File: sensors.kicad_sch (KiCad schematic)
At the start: 22 parts, among them J10 DISTANCE_R90, J11 DISTANCE_R, J12 DISTANCE_RF, J13 DISTANCE_L90, J14 DISTANCE_L, J15 LINE_LEFT, J16 DISTANCE_LF, J8 DISTANCE_CENTER, J9 LINE_RIGHT, U5 TXS0108EPWR

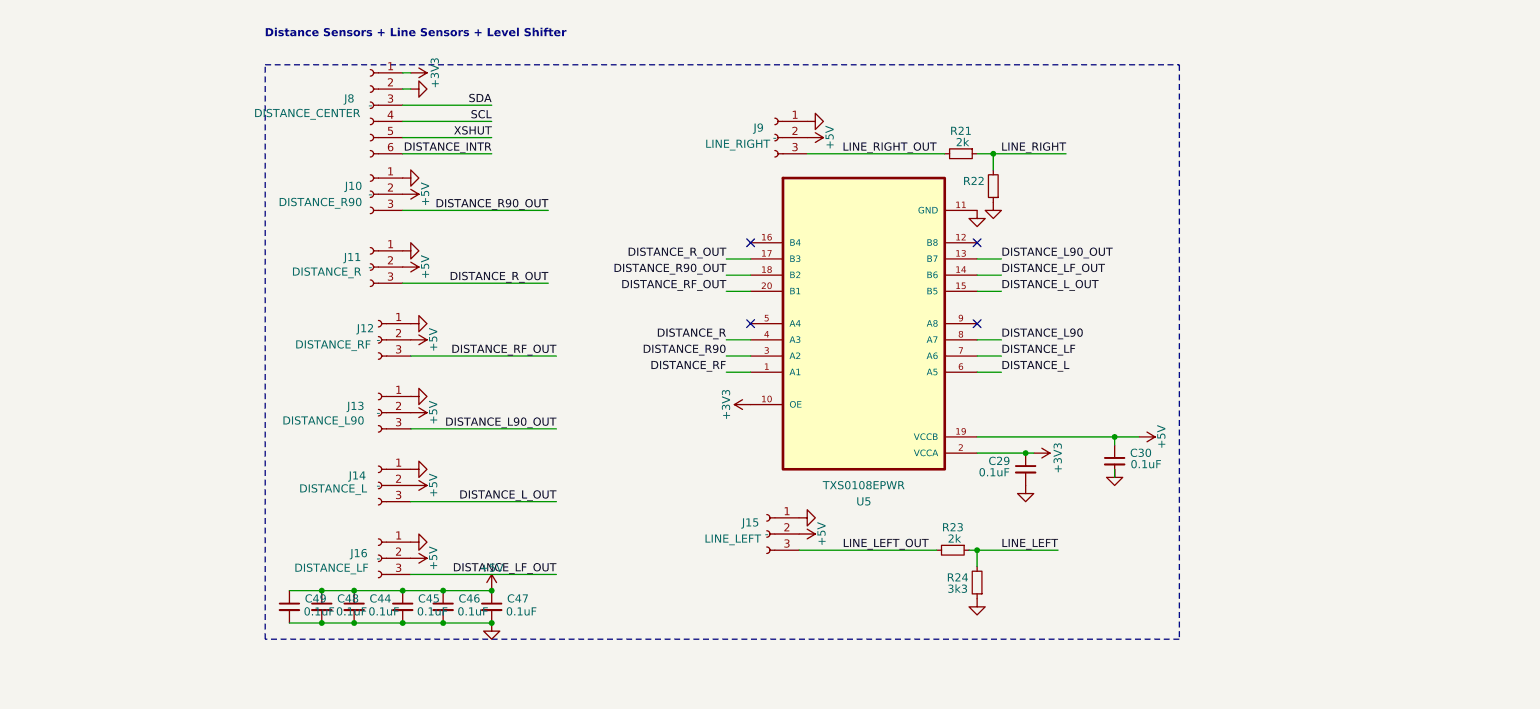
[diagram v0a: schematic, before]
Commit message: added global labels
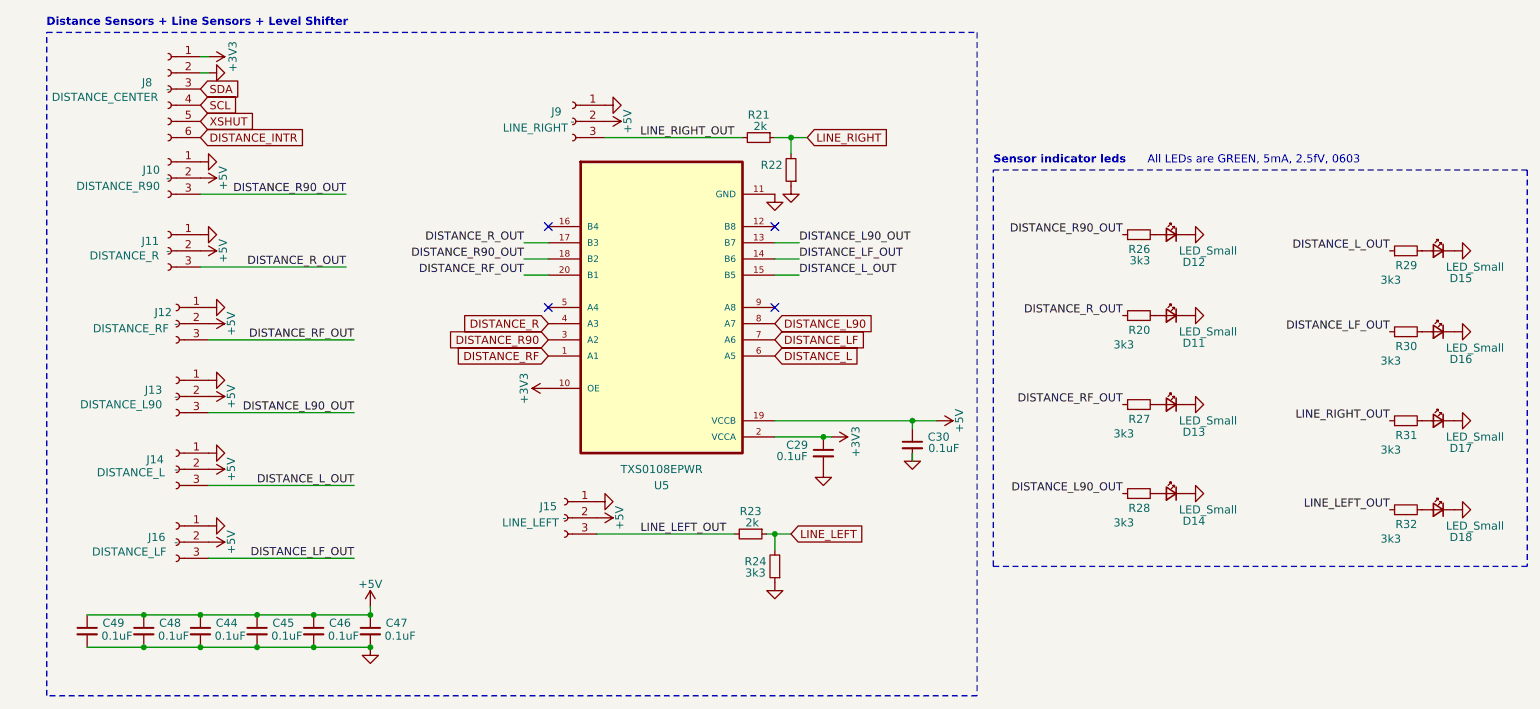
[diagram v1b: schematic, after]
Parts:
- added D11, D12, D13, D14, D15, D16, D17, D18: LED_Small, LED_SMD:LED_0603_1608Metric, symbol Device:LED_Small
- added R20, R26, R27, R28, R29, R30, R31, R32: 3k3, Resistor_SMD:R_0603_1608Metric, symbol Device:R_Small
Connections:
- net DISTANCE_L90_OUT: now also R28.1
- net DISTANCE_LF_OUT: now also R30.1
- net DISTANCE_L_OUT: now also R29.1
- net DISTANCE_R90_OUT: now also R26.1
- net DISTANCE_RF_OUT: now also R27.1
- net DISTANCE_R_OUT: now also R20.1
- net GND: now also D11.1 (K), D12.1 (K), D13.1 (K), D14.1 (K), D15.1 (K), D16.1 (K), D17.1 (K), D18.1 (K)
- net LINE_LEFT_OUT: now also R32.1
- net LINE_RIGHT_OUT: now also R31.1
- new net: D15.2 (A), R29.2
- new net: D13.2 (A), R27.2
- new net: D16.2 (A), R30.2
- new net: D12.2 (A), R26.2
- new net: D17.2 (A), R31.2
- new net: D11.2 (A), R20.2
- new net: D14.2 (A), R28.2
- new net: D18.2 (A), R32.2
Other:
- note added: "All LEDs are GREEN, 5mA, 2.5fV, 0603"
- note added: "Sensor indicator leds"
- moved on the sheet: C29, C30, C44, C45, C46, C47, C48, C49, J10, J11, J12, J13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

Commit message: added PDFs
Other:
- title: (none) -> Minisumo PCB
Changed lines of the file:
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@@
 	(generator_version "9.0")
 	(paper "A4")
+	(title_block
+		(title "Minisumo PCB")
+		(date "2025-04-16")
+		(rev "3.2")
+		(comment 2 "alex_ivan1304@outlook.com")
+		(comment 3 "Designed by: Ivan Alexandru Marian")
+	)
 	(rectangle
 		(start 189.23 72.39)

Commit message: custom
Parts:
- R21, R23: value 2k -> 1k
- R22, R24: value 3k3 -> 2k
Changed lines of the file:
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@@
 			)
 		)
-		(property "Value" "3k3"
+		(property "Value" "2k"
 			(at 154.432 73.406 0)
 			(effects
@@
 					(size 1.27 1.27)
 				)
-				(hide yes)
 			)
 		)
@@
 			)
 		)
-		(property "Value" "2k"
+		(property "Value" "1k"
 			(at 152.654 65.532 90)
 			(effects
@@
 			)
 		)
-		(property "Value" "2k"
+		(property "Value" "1k"
 			(at 151.384 127.762 90)
 			(effects
@@
 			)
 		)
-		(property "Value" "3k3"
+		(property "Value" "2k"
 			(at 151.892 135.636 0)
 			(effects
